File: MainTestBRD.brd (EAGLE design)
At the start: 100 x 80 mm, 39 parts, among them IC1 LM3940IMP-3.3, IC2 AT90CAN128, Q1 BC847BLT1SMD, Q2 BD139

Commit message: new version
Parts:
- moved C11 22.5 mm to (7.62, 38.4)
- moved C13 22.5 mm to (44.5, 30.8)
- moved C2 22.5 mm to (44.5, 33.4)
- moved C3 22.5 mm to (44.5, 35.9)
- moved C4 22.5 mm to (8.89, 21.9)
- moved C6 22.5 mm to (8.89, 15.6)
- moved C7 22.5 mm to (12.7, 13.0)
- moved JP3 22.5 mm to (20.3, 53.7)
- moved JP4 22.5 mm to (8.89, 44.8)
- moved LED3 22.5 mm to (15.2, 38.4)
- moved Q2 22.5 mm to (35.6, 35.9)
- moved R1 22.5 mm to (26.7, 38.4)
- moved R3 22.5 mm to (50.8, 30.8)
- moved R5 22.5 mm to (20.3, 38.4)
- moved S1 22.5 mm to (39.4, 53.7)
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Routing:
- net N$16: track 18.9 -> 6.94 mm, vias 1 -> 0
- net N$12: track 22.5 -> 33.8 mm, vias 0 -> 2
- net GND: track 302.1 -> 312.7 mm, vias 2 -> 1
- net N$19: track 13.4 -> 4.06 mm, vias 1 -> 0
- net AGND: track 152.2 -> 145.4 mm
- net VDD: track 114.2 -> 120.4 mm
- net VCC: track 157.6 -> 160.2 mm
- net N$27: track 2.38 -> 0.00 mm
- net N$15: track 13.6 -> 15.5 mm
- net N$21: track 15.4 -> 13.8 mm, vias 2 -> 1
- net N$22: track 13.8 -> 15.4 mm
- net BT_WAKE_HW: track 23.4 -> 24.6 mm, vias 1 -> 0
- net BT_TX: track 25.3 -> 24.3 mm
- net N$6: track 17.8 -> 17.9 mm, vias 1 -> 0
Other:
- board size 100 x 80 mm -> 100.2 x 57.5 mm
- board text added: "BT Head MDSoft R 3.0"

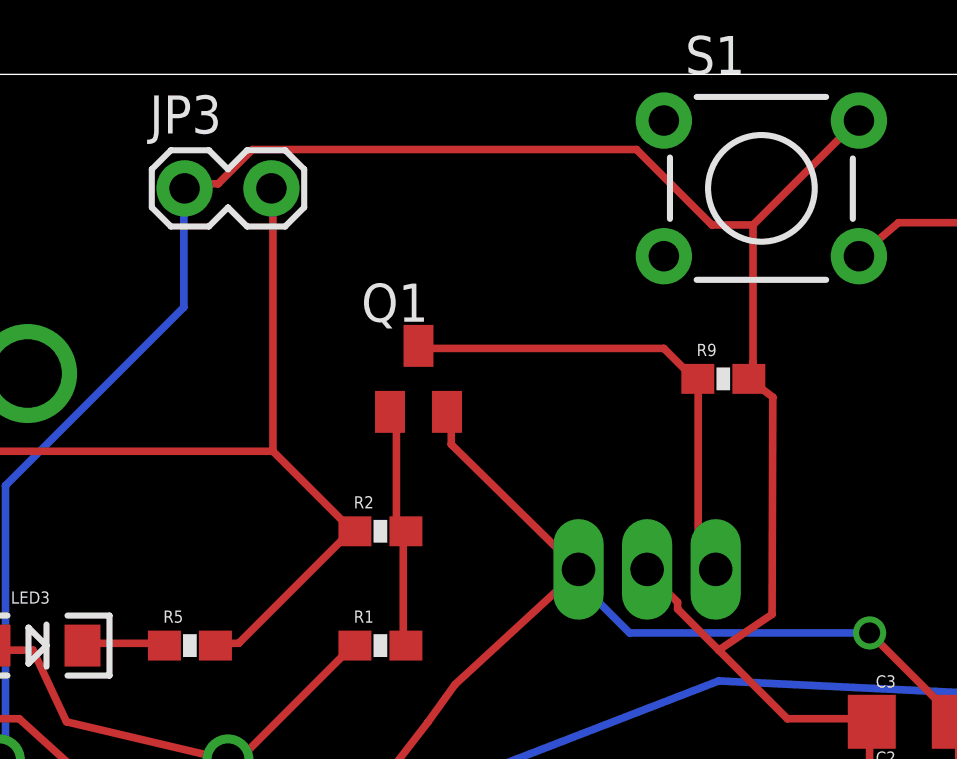
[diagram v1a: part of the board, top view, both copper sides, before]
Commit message: DTA143ZKA needs
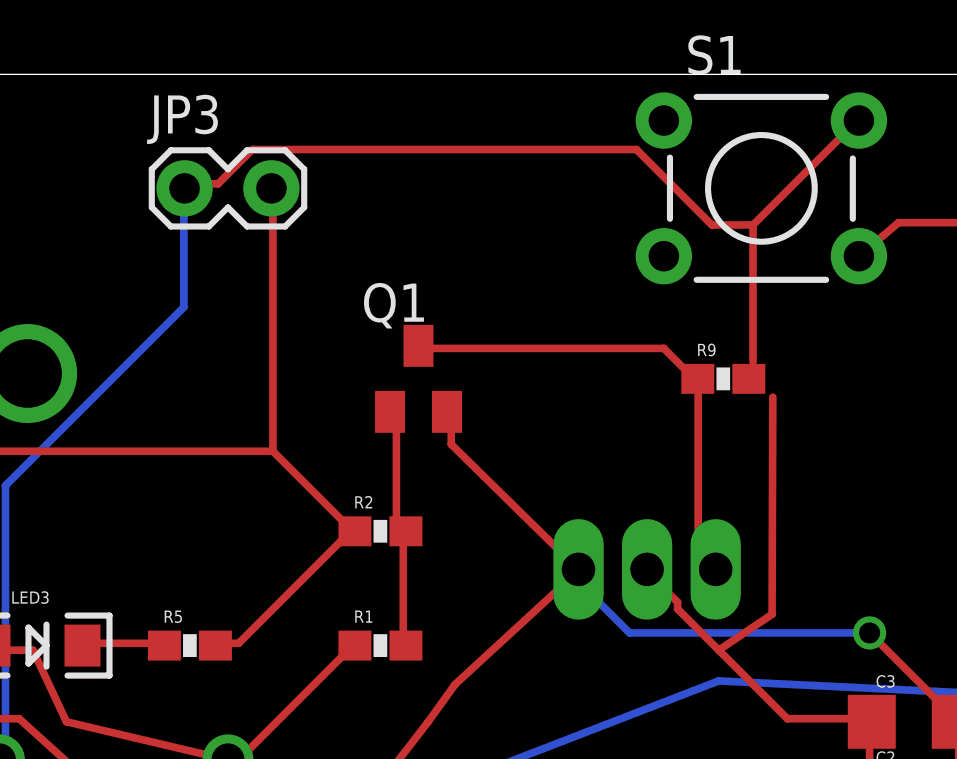
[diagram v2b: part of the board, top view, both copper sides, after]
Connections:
- new net N$30: JP3.1, Q2.2, R9.2
- new net N$31: Q2.1
- net GND: no longer Q2.1
- net VCC: no longer JP3.1, Q2.2, R9.2
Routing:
- net VCC: track 160.2 -> 158.1 mm
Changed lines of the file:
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@@
 <?xml version="1.0" encoding="utf-8"?>
 <!DOCTYPE eagle SYSTEM "eagle.dtd">
-<eagle version="7.2.0">
+<eagle version="7.1.0">
 <drawing>
 <settings>
@@
 <contactref element="IC2" pad="53"/>
 <contactref element="Q1" pad="2"/>
-<contactref element="Q2" pad="1"/>
 <contactref element="R2" pad="1"/>
 <contactref element="JP3" pad="2"/>
@@
 <wire x1="33.2994" y1="40.9546" x2="29.0322" y2="45.1456" width="0.254" layer="1"/>
 <wire x1="29.0322" y1="46.06" x2="28.89" y2="46.23" width="0.254" layer="1"/>
-<wire x1="33.147" y1="41.0308" x2="33.274" y2="40.98" width="0.254" layer="1"/>
 <wire x1="6.4008" y1="33.9442" x2="6.4008" y2="36.0016" width="0.254" layer="1"/>
 <wire x1="6.4008" y1="36.0016" x2="6.4008" y2="38.2876" width="0.254" layer="1"/>
@@
 <wire x1="14.6304" y1="36.0016" x2="18.3896" y2="32.598" width="0.254" layer="1"/>
 <wire x1="6.4008" y1="36.0016" x2="14.6304" y2="36.0016" width="0.254" layer="1"/>
-<wire x1="33.2994" y1="40.9546" x2="33.274" y2="40.98" width="0.254" layer="1"/>
 <wire x1="10.287" y1="44.917" x2="23.0886" y2="44.917" width="0.254" layer="1"/>
 <wire x1="10.287" y1="44.917" x2="10.14" y2="44.79" width="0.254" layer="1"/>
@@
 <wire x1="33.3756" y1="40.9194" x2="33.3756" y2="40.4622" width="0.254" layer="16"/>
 <wire x1="45.72" y1="36.1188" x2="45.85" y2="35.9" width="0.254" layer="1"/>
-<wire x1="33.3756" y1="40.9194" x2="33.274" y2="40.98" width="0.254" layer="16"/>
 <wire x1="35.8902" y1="24.6888" x2="26.7462" y2="33.8328" width="0.254" layer="1"/>
 <wire x1="37.9476" y1="24.6888" x2="35.8902" y2="24.6888" width="0.254" layer="1"/>
@@
 <wire x1="37.9476" y1="24.6888" x2="38.1" y2="24.47" width="0.254" layer="1"/>
 <via x="42.9768" y="38.862" extent="1-16" drill="0.7"/>
+<wire x1="33.2994" y1="40.9546" x2="33.3756" y2="40.9194" width="0" layer="19" extent="1-16"/>
 </signal>
 <signal name="N$8">
@@
 <contactref element="JP2" pad="7"/>
 <contactref element="UF4001" pad="C"/>
-<contactref element="Q2" pad="2"/>
-<contactref element="R9" pad="2"/>
-<contactref element="JP3" pad="1"/>
 <contactref element="IC2" pad="52"/>
 <contactref element="IC2" pad="21"/>
@@
 <wire x1="37.9476" y1="38.2876" x2="36.576" y2="39.6592" width="0.254" layer="1"/>
 <wire x1="42.9768" y1="36.0016" x2="40.2336" y2="36.0016" width="0.254" layer="1"/>
-<wire x1="35.6616" y1="40.8022" x2="35.56" y2="40.98" width="0.254" layer="1"/>
 <wire x1="42.9768" y1="36.0016" x2="43.05" y2="35.9" width="0.254" layer="1"/>
 <wire x1="39.0906" y1="52.4608" x2="39.0906" y2="47.8888" width="0.254" layer="1"/>
 <wire x1="42.5196" y1="55.8898" x2="39.0906" y2="52.4608" width="0.254" layer="1"/>
-<wire x1="39.0906" y1="47.8888" x2="38.95" y2="47.33" width="0.254" layer="1"/>
 <wire x1="42.5196" y1="55.8898" x2="42.6212" y2="55.9406" width="0.254" layer="1"/>
 <wire x1="21.2598" y1="53.8324" x2="20.3454" y2="53.8324" width="0.254" layer="1"/>
@@
 <wire x1="37.719" y1="52.4608" x2="35.2044" y2="54.9754" width="0.254" layer="1"/>
 <wire x1="39.0906" y1="52.4608" x2="37.719" y2="52.4608" width="0.254" layer="1"/>
-<wire x1="20.3454" y1="53.8324" x2="20.1422" y2="53.68" width="0.254" layer="1"/>
 <wire x1="39.7256" y1="39.4814" x2="37.9476" y2="38.2876" width="0.254" layer="1"/>
 <wire x1="39.751" y1="46.7204" x2="39.7256" y2="39.4814" width="0.254" layer="1"/>
-<wire x1="39.751" y1="46.7204" x2="38.95" y2="47.33" width="0.254" layer="1"/>
 <wire x1="20.1168" y1="49.7176" x2="14.1732" y2="43.774" width="0.254" layer="16"/>
 <wire x1="20.1168" y1="53.6038" x2="20.1168" y2="49.7176" width="0.254" layer="16"/>
 <wire x1="14.1732" y1="34.63" x2="13.97" y2="34.63" width="0.254" layer="16"/>
-<wire x1="20.1168" y1="53.6038" x2="20.1422" y2="53.68" width="0.254" layer="16"/>
 <wire x1="45.9486" y1="16.6878" x2="40.6908" y2="16.6878" width="0.254" layer="16"/>
 <wire x1="47.5488" y1="15.0876" x2="45.9486" y2="16.6878" width="0.254" layer="16"/>
@@
 <wire x1="48.96" y1="12.33" x2="48.96" y2="13.2096" width="0.4064" layer="1"/>
 <wire x1="48.96" y1="13.2096" x2="49.2706" y2="13.5202" width="0.4064" layer="1"/>
+<wire x1="20.1168" y1="53.6038" x2="20.3454" y2="53.8324" width="0" layer="19" extent="1-16"/>
+<wire x1="39.751" y1="46.7204" x2="39.0906" y2="47.8888" width="0" layer="19" extent="1-1"/>
 </signal>
 <signal name="XTAL1">
@@
 <via x="48.73" y="16.56" extent="1-16" drill="0.7"/>
 </signal>
+<signal name="N$30">
+<contactref element="R9" pad="2"/>
+<contactref element="JP3" pad="1"/>
+<contactref element="Q2" pad="2"/>
+<wire x1="35.56" y1="40.98" x2="38.95" y2="47.33" width="0" layer="19" extent="1-1"/>
+<wire x1="20.1422" y1="53.68" x2="38.95" y2="47.33" width="0" layer="19" extent="1-1"/>
+</signal>
+<signal name="N$31">
+<contactref element="Q2" pad="1"/>
+</signal>
 </signals>
